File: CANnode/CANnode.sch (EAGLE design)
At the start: 245 parts, among them IC1 ISO1050DUB, IC2 ISO1050DUB, Q1 FDV302P, Q3 FDV302P, U1 LM324PW, U10 FT2232HL, U11 93LC56C-I/SN, U2 TPS70445_PWP_24, U3 LM324PW, U4 LM324PW, U5 LM324PW, U6 LM324PW, U7 RM42L432_PZ_100RM42L432_PZ_100, U8 LM324PW, U9 XC2C32A-6CP56C, X1 AS14-35, Y1 12M

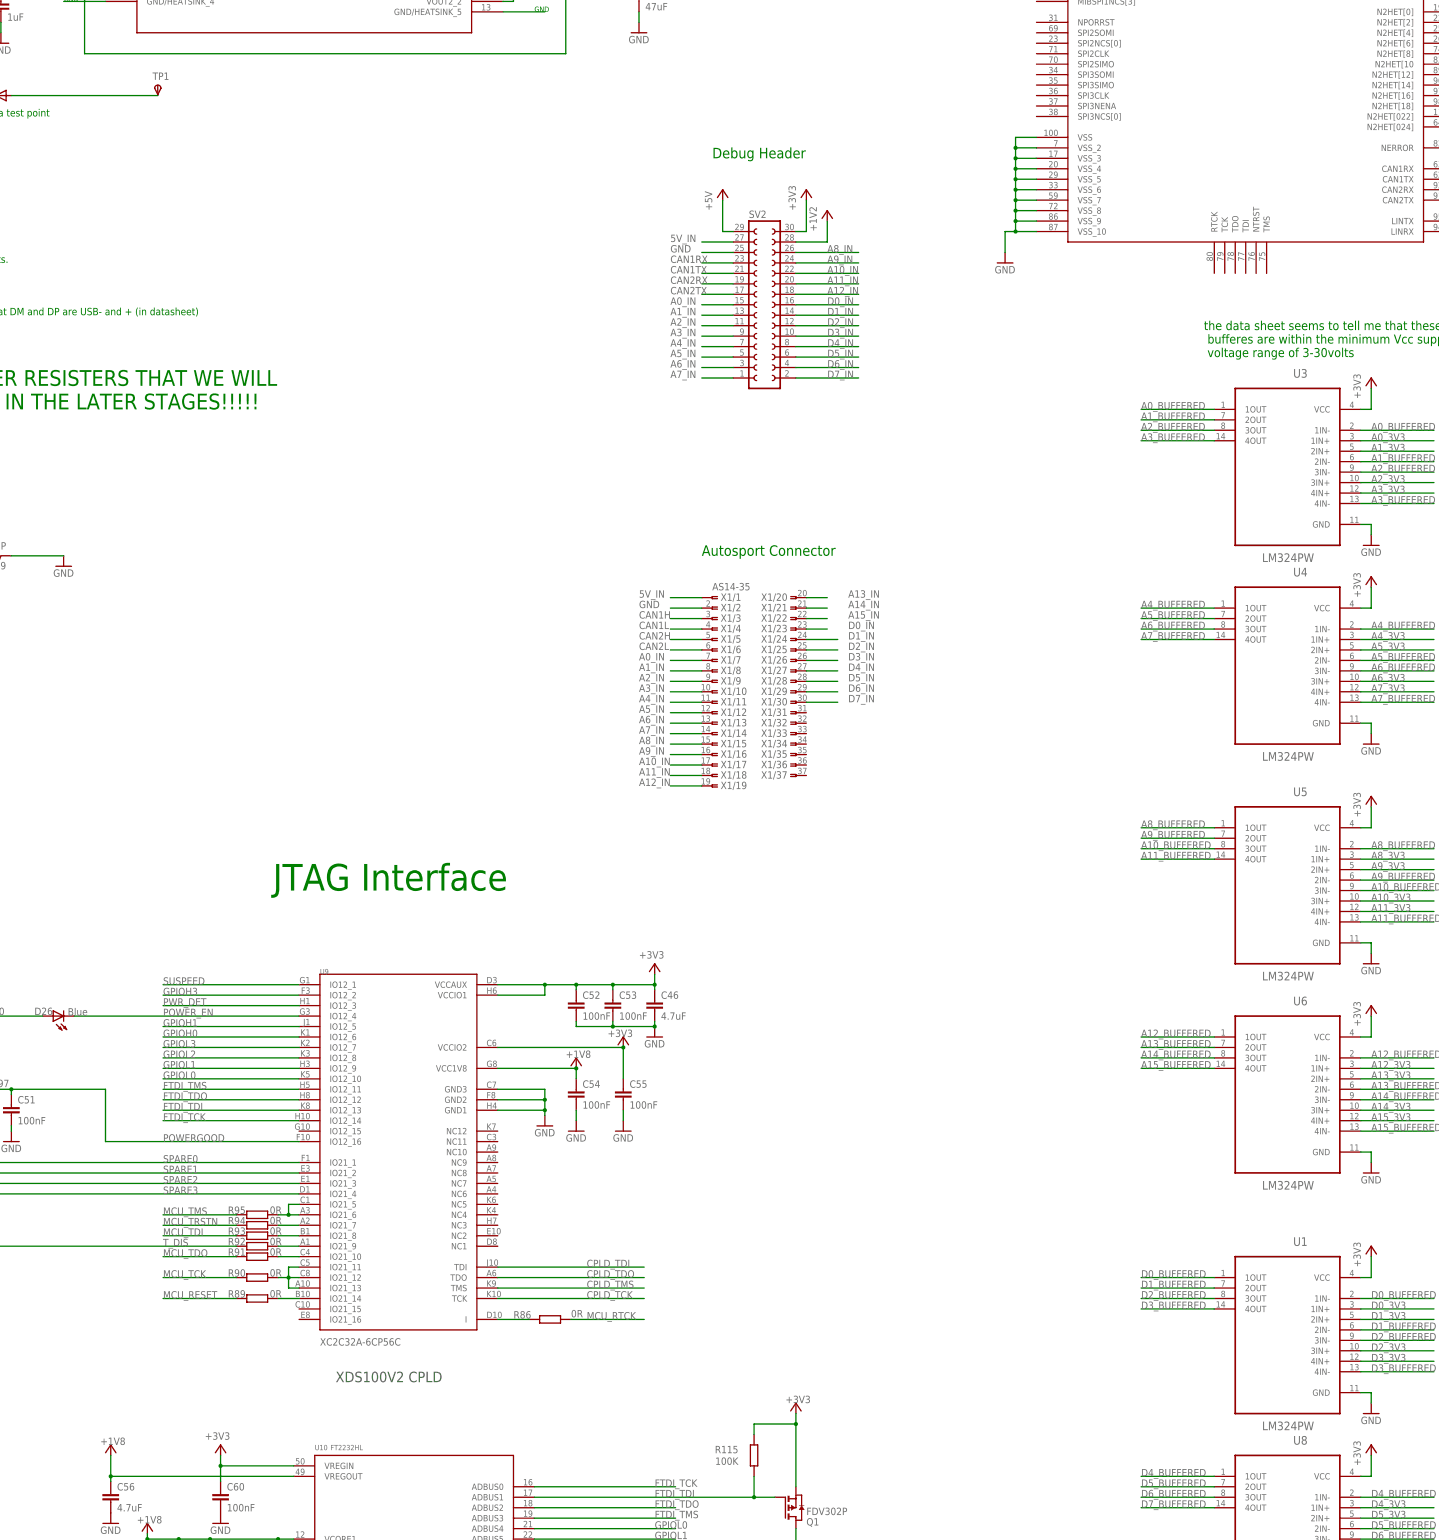
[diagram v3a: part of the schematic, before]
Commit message: played with vias and routing
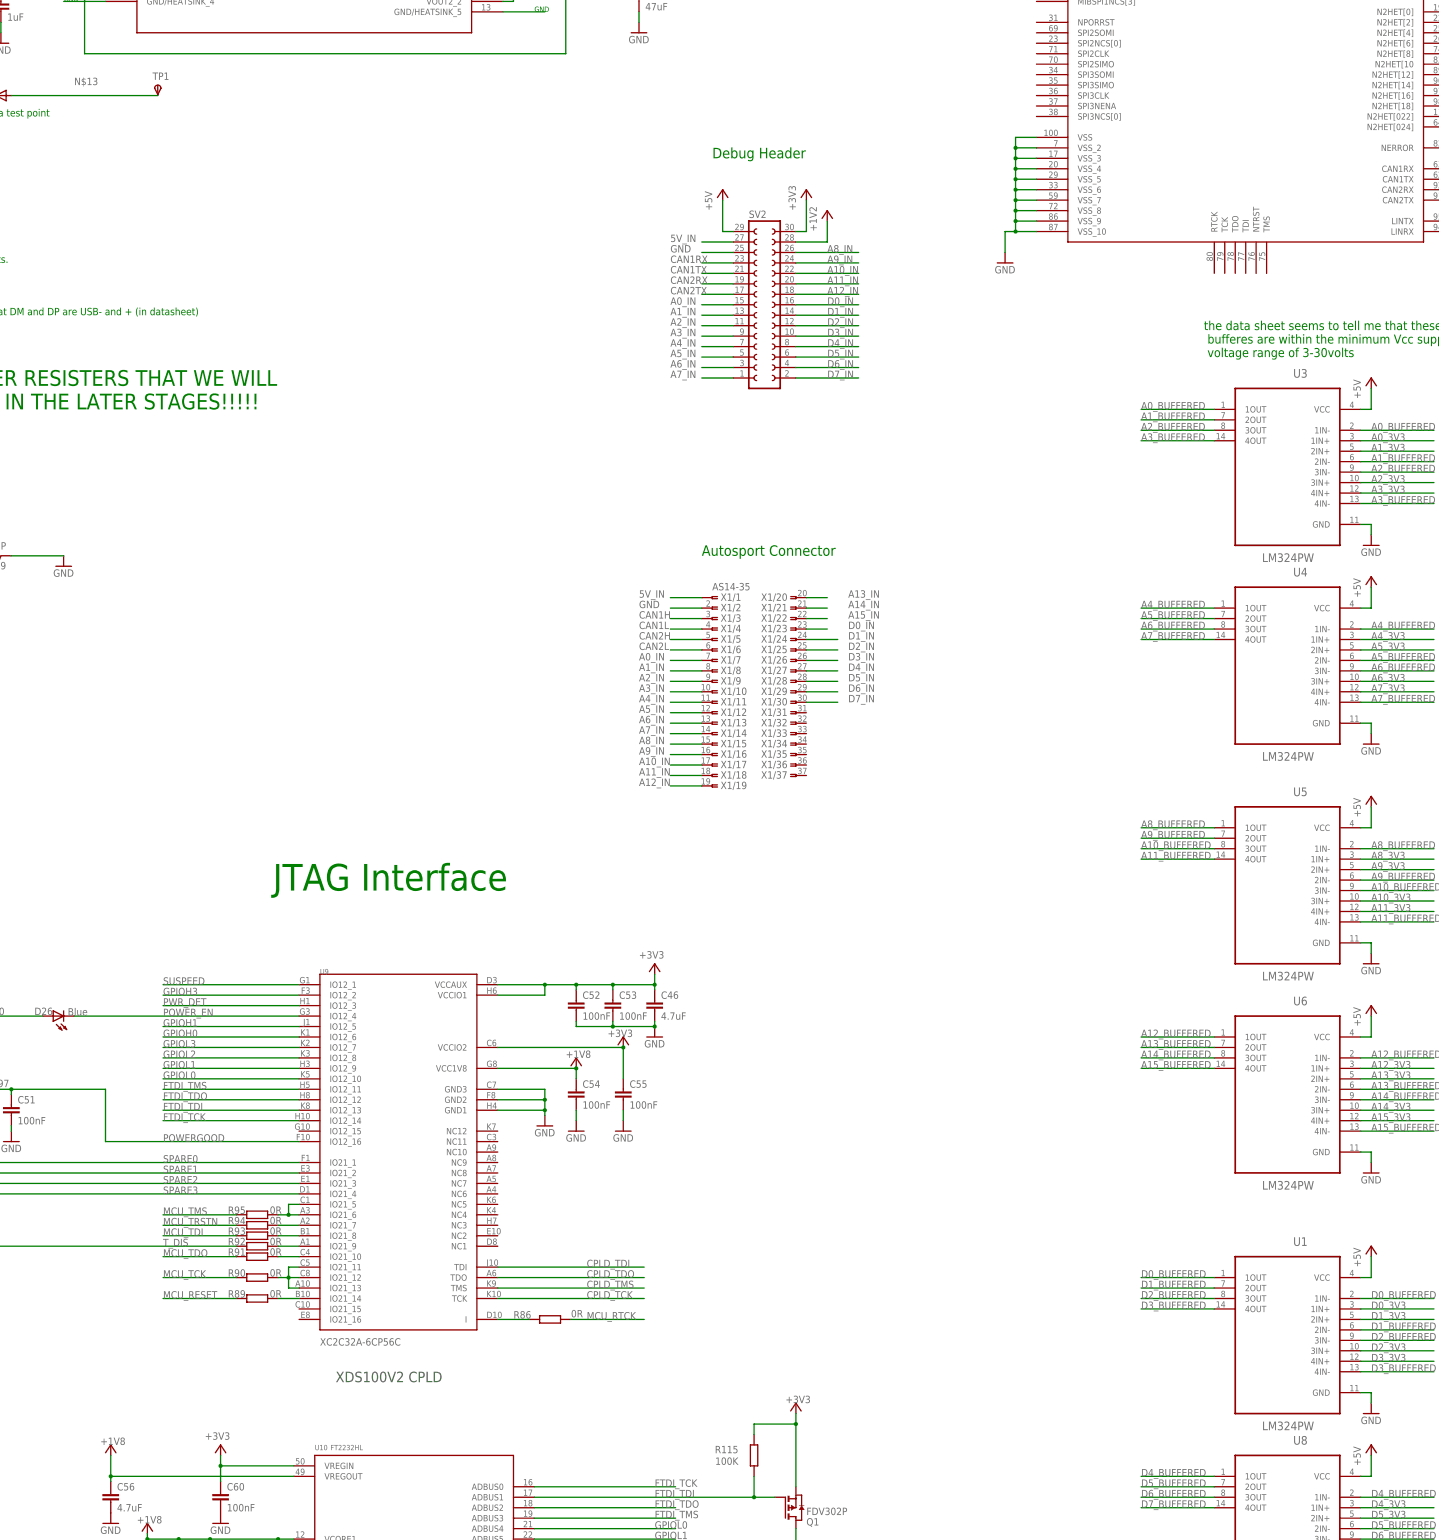
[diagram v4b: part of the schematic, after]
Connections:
- net +3V3: no longer U1.VCC, U3.VCC, U4.VCC, U5.VCC, U6.VCC, U8.VCC
- net +5V: now also U1.VCC, U3.VCC, U4.VCC, U5.VCC, U6.VCC, U8.VCC
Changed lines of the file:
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@@
 <classes>
 <class number="0" name="default" width="0" drill="0">
+<clearance class="0" value="0.205"/>
 </class>
 </classes>
@@
 <part name="GND12" library="supply1" deviceset="GND" device=""/>
 <part name="GND14" library="supply1" deviceset="GND" device=""/>
-<part name="+3V7" library="supply1" deviceset="+3V3" device=""/>
-<part name="+3V8" library="supply1" deviceset="+3V3" device=""/>
-<part name="+3V11" library="supply1" deviceset="+3V3" device=""/>
-<part name="+3V12" library="supply1" deviceset="+3V3" device=""/>
-<part name="+3V13" library="supply1" deviceset="+3V3" device=""/>
-<part name="+3V9" library="supply1" deviceset="+3V3" device=""/>
 <part name="D2" library="eagle-ltspice" deviceset="R" device="R0402" value="TVS DIODE"/>
 <part name="D3" library="eagle-ltspice" deviceset="R" device="R0402" value="TVS DIODE"/>
@@
 <part name="R59" library="resistor" deviceset="R-US_" device="R0402" value="DNP"/>
 <part name="GND120" library="supply1" deviceset="GND" device=""/>
+<part name="P+5" library="supply1" deviceset="+5V" device=""/>
+<part name="P+6" library="supply1" deviceset="+5V" device=""/>
+<part name="P+7" library="supply1" deviceset="+5V" device=""/>
+<part name="P+9" library="supply1" deviceset="+5V" device=""/>
+<part name="P+10" library="supply1" deviceset="+5V" device=""/>
+<part name="P+11" library="supply1" deviceset="+5V" device=""/>
 </parts>
 <sheets>
@@
 <instance part="GND12" gate="1" x="497.84" y="-33.02"/>
 <instance part="GND14" gate="1" x="469.9" y="-50.8"/>
-<instance part="+3V7" gate="G$1" x="411.48" y="-101.6"/>
-<instance part="+3V8" gate="G$1" x="411.48" y="-149.86"/>
-<instance part="+3V11" gate="G$1" x="411.48" y="-254"/>
-<instance part="+3V12" gate="G$1" x="411.48" y="-312.42"/>
-<instance part="+3V13" gate="G$1" x="411.48" y="-360.68"/>
-<instance part="+3V9" gate="G$1" x="411.48" y="-203.2"/>
 <instance part="D2" gate="G$1" x="10.16" y="-96.52" rot="R90"/>
 <instance part="D3" gate="G$1" x="17.78" y="-96.52" rot="R90"/>
@@
 <instance part="R59" gate="G$1" x="76.2" y="-144.78" rot="R180"/>
 <instance part="GND120" gate="1" x="93.98" y="-147.32"/>
+<instance part="P+5" gate="1" x="411.48" y="-101.6"/>
+<instance part="P+6" gate="1" x="411.48" y="-149.86"/>
+<instance part="P+7" gate="1" x="411.48" y="-203.2"/>
+<instance part="P+9" gate="1" x="411.48" y="-254"/>
+<instance part="P+10" gate="1" x="411.48" y="-312.42"/>
+<instance part="P+11" gate="1" x="411.48" y="-360.68"/>
 </instances>
 <busses>
@@
 </segment>
 <segment>
-<pinref part="U3" gate="A" pin="VCC"/>
-<wire x1="408.94" y1="-109.22" x2="411.48" y2="-109.22" width="0.1524" layer="91"/>
-<wire x1="411.48" y1="-109.22" x2="411.48" y2="-104.14" width="0.1524" layer="91"/>
-<pinref part="+3V7" gate="G$1" pin="+3V3"/>
-</segment>
-<segment>
-<pinref part="U4" gate="A" pin="VCC"/>
-<wire x1="408.94" y1="-157.48" x2="411.48" y2="-157.48" width="0.1524" layer="91"/>
-<wire x1="411.48" y1="-157.48" x2="411.48" y2="-152.4" width="0.1524" layer="91"/>
-<pinref part="+3V8" gate="G$1" pin="+3V3"/>
-</segment>
-<segment>
-<pinref part="U6" gate="A" pin="VCC"/>
-<wire x1="408.94" y1="-261.62" x2="411.48" y2="-261.62" width="0.1524" layer="91"/>
-<wire x1="411.48" y1="-261.62" x2="411.48" y2="-256.54" width="0.1524" layer="91"/>
-<pinref part="+3V11" gate="G$1" pin="+3V3"/>
-</segment>
-<segment>
-<pinref part="U1" gate="A" pin="VCC"/>
-<wire x1="408.94" y1="-320.04" x2="411.48" y2="-320.04" width="0.1524" layer="91"/>
-<wire x1="411.48" y1="-320.04" x2="411.48" y2="-314.96" width="0.1524" layer="91"/>
-<pinref part="+3V12" gate="G$1" pin="+3V3"/>
-</segment>
-<segment>
-<pinref part="U8" gate="A" pin="VCC"/>
-<wire x1="408.94" y1="-368.3" x2="411.48" y2="-368.3" width="0.1524" layer="91"/>
-<wire x1="411.48" y1="-368.3" x2="411.48" y2="-363.22" width="0.1524" layer="91"/>
-<pinref part="+3V13" gate="G$1" pin="+3V3"/>
-</segment>
-<segment>
-<pinref part="U5" gate="A" pin="VCC"/>
-<wire x1="408.94" y1="-210.82" x2="411.48" y2="-210.82" width="0.1524" layer="91"/>
-<wire x1="411.48" y1="-210.82" x2="411.48" y2="-205.74" width="0.1524" layer="91"/>
-<pinref part="+3V9" gate="G$1" pin="+3V3"/>
-</segment>
-<segment>
 <pinref part="+3V10" gate="G$1" pin="+3V3"/>
 <wire x1="274.32" y1="-58.42" x2="274.32" y2="-66.04" width="0.1524" layer="91"/>
@@
 <wire x1="81.28" y1="-33.02" x2="116.84" y2="-33.02" width="0.1524" layer="91"/>
 <pinref part="TP1" gate="G$1" pin="PP"/>
+<label x="96.52" y="-30.48" size="1.778" layer="95"/>
 </segment>
 </net>
@@
 <wire x1="254" y1="-66.04" x2="254" y2="-58.42" width="0.1524" layer="91"/>
 </segment>
+<segment>
+<pinref part="U3" gate="A" pin="VCC"/>
+<wire x1="408.94" y1="-109.22" x2="411.48" y2="-109.22" width="0.1524" layer="91"/>
+<wire x1="411.48" y1="-109.22" x2="411.48" y2="-104.14" width="0.1524" layer="91"/>
+<pinref part="P+5" gate="1" pin="+5V"/>
+</segment>
+<segment>
+<pinref part="U4" gate="A" pin="VCC"/>
+<wire x1="408.94" y1="-157.48" x2="411.48" y2="-157.48" width="0.1524" layer="91"/>
+<wire x1="411.48" y1="-157.48" x2="411.48" y2="-152.4" width="0.1524" layer="91"/>
+<pinref part="P+6" gate="1" pin="+5V"/>
+</segment>
+<segment>
+<pinref part="U5" gate="A" pin="VCC"/>
+<wire x1="408.94" y1="-210.82" x2="411.48" y2="-210.82" width="0.1524" layer="91"/>
+<wire x1="411.48" y1="-210.82" x2="411.48" y2="-205.74" width="0.1524" layer="91"/>
+<pinref part="P+7" gate="1" pin="+5V"/>
+</segment>
+<segment>
+<pinref part="U1" gate="A" pin="VCC"/>
+<wire x1="408.94" y1="-320.04" x2="411.48" y2="-320.04" width="0.1524" layer="91"/>
+<wire x1="411.48" y1="-320.04" x2="411.48" y2="-314.96" width="0.1524" layer="91"/>
+<pinref part="P+10" gate="1" pin="+5V"/>
+</segment>
+<segment>
+<pinref part="U8" gate="A" pin="VCC"/>
+<wire x1="408.94" y1="-368.3" x2="411.48" y2="-368.3" width="0.1524" layer="91"/>
+<wire x1="411.48" y1="-368.3" x2="411.48" y2="-363.22" width="0.1524" layer="91"/>
+<pinref part="P+11" gate="1" pin="+5V"/>
+</segment>
+<segment>
+<pinref part="U6" gate="A" pin="VCC"/>
+<wire x1="408.94" y1="-261.62" x2="411.48" y2="-261.62" width="0.1524" layer="91"/>
+<wire x1="411.48" y1="-261.62" x2="411.48" y2="-256.54" width="0.1524" layer="91"/>
+<pinref part="P+9" gate="1" pin="+5V"/>
+</segment>
 </net>

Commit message: Added another layer (Power)
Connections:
- net +5V: now also C1.1, C2.1, C5.+, C6.1, F1.2, R3.2, U2.VIN1, U2.VIN1_2, U2.VIN2, U2.VIN2_2
- net 3.3V: no longer C1.1, C2.1, C5.+, C6.1, F1.2, R3.2, U2.VIN1, U2.VIN1_2, U2.VIN2, U2.VIN2_2
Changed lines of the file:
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@@
 <pinref part="IC1" gate="G$1" pin="VCC2"/>
-</segment>
-<segment>
-<pinref part="U2" gate="A" pin="VIN1"/>
-<wire x1="104.14" y1="12.7" x2="101.6" y2="12.7" width="0.1524" layer="91"/>
-<pinref part="U2" gate="A" pin="VIN1_2"/>
-<wire x1="101.6" y1="12.7" x2="78.74" y2="12.7" width="0.1524" layer="91"/>
-<wire x1="104.14" y1="15.24" x2="101.6" y2="15.24" width="0.1524" layer="91"/>
-<wire x1="101.6" y1="15.24" x2="101.6" y2="12.7" width="0.1524" layer="91"/>
-<junction x="101.6" y="12.7"/>
-<pinref part="C1" gate="G$1" pin="1"/>
-<pinref part="U2" gate="A" pin="VIN2"/>
-<wire x1="104.14" y1="-7.62" x2="101.6" y2="-7.62" width="0.1524" layer="91"/>
-<pinref part="U2" gate="A" pin="VIN2_2"/>
-<wire x1="101.6" y1="-7.62" x2="78.74" y2="-7.62" width="0.1524" layer="91"/>
-<wire x1="104.14" y1="-5.08" x2="101.6" y2="-5.08" width="0.1524" layer="91"/>
-<wire x1="101.6" y1="-5.08" x2="101.6" y2="-7.62" width="0.1524" layer="91"/>
-<junction x="101.6" y="-7.62"/>
-<pinref part="C2" gate="G$1" pin="1"/>
-<wire x1="78.74" y1="-7.62" x2="68.58" y2="-7.62" width="0.1524" layer="91"/>
-<wire x1="68.58" y1="-7.62" x2="68.58" y2="12.7" width="0.1524" layer="91"/>
-<junction x="78.74" y="-7.62"/>
-<wire x1="78.74" y1="12.7" x2="68.58" y2="12.7" width="0.1524" layer="91"/>
-<junction x="78.74" y="12.7"/>
-<junction x="68.58" y="12.7"/>
-<wire x1="68.58" y1="12.7" x2="50.8" y2="12.7" width="0.1524" layer="91"/>
-<pinref part="F1" gate="G$1" pin="2"/>
-<pinref part="R3" gate="G$1" pin="2"/>
-<wire x1="50.8" y1="12.7" x2="40.64" y2="12.7" width="0.1524" layer="91"/>
-<wire x1="40.64" y1="12.7" x2="30.48" y2="12.7" width="0.1524" layer="91"/>
-<wire x1="30.48" y1="12.7" x2="20.32" y2="12.7" width="0.1524" layer="91"/>
-<wire x1="30.48" y1="10.16" x2="30.48" y2="12.7" width="0.1524" layer="91"/>
-<junction x="30.48" y="12.7"/>
-<pinref part="P+3" gate="1" pin="+5V"/>
-<wire x1="30.48" y1="12.7" x2="30.48" y2="20.32" width="0.1524" layer="91"/>
-<pinref part="C5" gate="G$1" pin="+"/>
-<wire x1="40.64" y1="7.62" x2="40.64" y2="12.7" width="0.1524" layer="91"/>
-<junction x="40.64" y="12.7"/>
-<pinref part="C6" gate="G$1" pin="1"/>
-<wire x1="50.8" y1="7.62" x2="50.8" y2="12.7" width="0.1524" layer="91"/>
-<junction x="50.8" y="12.7"/>
 </segment>
 </net>
@@
 <pinref part="P+9" gate="1" pin="+5V"/>
 </segment>
-</net>
+<segment>
+<pinref part="U2" gate="A" pin="VIN1"/>
+<wire x1="104.14" y1="12.7" x2="101.6" y2="12.7" width="0.1524" layer="91"/>
+<pinref part="U2" gate="A" pin="VIN1_2"/>
+<wire x1="101.6" y1="12.7" x2="78.74" y2="12.7" width="0.1524" layer="91"/>
+<wire x1="104.14" y1="15.24" x2="101.6" y2="15.24" width="0.1524" layer="91"/>
+<wire x1="101.6" y1="15.24" x2="101.6" y2="12.7" width="0.1524" layer="91"/>
+<junction x="101.6" y="12.7"/>
+<pinref part="C1" gate="G$1" pin="1"/>
+<pinref part="U2" gate="A" pin="VIN2"/>
+<wire x1="104.14" y1="-7.62" x2="101.6" y2="-7.62" width="0.1524" layer="91"/>
+<pinref part="U2" gate="A" pin="VIN2_2"/>
+<wire x1="101.6" y1="-7.62" x2="78.74" y2="-7.62" width="0.1524" layer="91"/>
+<wire x1="104.14" y1="-5.08" x2="101.6" y2="-5.08" width="0.1524" layer="91"/>
+<wire x1="101.6" y1="-5.08" x2="101.6" y2="-7.62" width="0.1524" layer="91"/>
+<junction x="101.6" y="-7.62"/>
+<pinref part="C2" gate="G$1" pin="1"/>
+<wire x1="78.74" y1="-7.62" x2="68.58" y2="-7.62" width="0.1524" layer="91"/>
+<wire x1="68.58" y1="-7.62" x2="68.58" y2="12.7" width="0.1524" layer="91"/>
+<junction x="78.74" y="-7.62"/>
+<wire x1="78.74" y1="12.7" x2="68.58" y2="12.7" width="0.1524" layer="91"/>
+<junction x="78.74" y="12.7"/>
+<junction x="68.58" y="12.7"/>
+<wire x1="68.58" y1="12.7" x2="50.8" y2="12.7" width="0.1524" layer="91"/>
+<pinref part="F1" gate="G$1" pin="2"/>
+<pinref part="R3" gate="G$1" pin="2"/>
+<wire x1="50.8" y1="12.7" x2="40.64" y2="12.7" width="0.1524" layer="91"/>
+<wire x1="40.64" y1="12.7" x2="30.48" y2="12.7" width="0.1524" layer="91"/>
+<wire x1="30.48" y1="12.7" x2="20.32" y2="12.7" width="0.1524" layer="91"/>
+<wire x1="30.48" y1="10.16" x2="30.48" y2="12.7" width="0.1524" layer="91"/>
+<junction x="30.48" y="12.7"/>
+<pinref part="P+3" gate="1" pin="+5V"/>
+<wire x1="30.48" y1="12.7" x2="30.48" y2="20.32" width="0.1524" layer="91"/>
+<pinref part="C5" gate="G$1" pin="+"/>
+<wire x1="40.64" y1="7.62" x2="40.64" y2="12.7" width="0.1524" layer="91"/>
+<junction x="40.64" y="12.7"/>
+<pinref part="C6" gate="G$1" pin="1"/>
+<wire x1="50.8" y1="7.62" x2="50.8" y2="12.7" width="0.1524" layer="91"/>
+<junction x="50.8" y="12.7"/>
+</segment>
+</net>

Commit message: Connected +5V
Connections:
- removed net 3.3V: C10.1, C9.1, IC1.VCC2, IC2.VCC2
- net +5V: now also C10.1, C9.1, IC1.VCC2, IC2.VCC2
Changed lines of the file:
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@@
-</segment>
-</net>
-<net name="3.3V" class="0">
-<segment>
-<wire x1="505.46" y1="-40.64" x2="505.46" y2="-20.32" width="0.1524" layer="91"/>
-<pinref part="C10" gate="G$1" pin="1"/>
-<wire x1="505.46" y1="-20.32" x2="497.84" y2="-20.32" width="0.1524" layer="91"/>
-<wire x1="497.84" y1="-20.32" x2="497.84" y2="-22.86" width="0.1524" layer="91"/>
-<pinref part="P+2" gate="1" pin="+5V"/>
-<wire x1="497.84" y1="-20.32" x2="497.84" y2="-17.78" width="0.1524" layer="91"/>
-<junction x="497.84" y="-20.32"/>
-<pinref part="IC2" gate="G$1" pin="VCC2"/>
-<wire x1="502.92" y1="-40.64" x2="505.46" y2="-40.64" width="0.1524" layer="91"/>
-</segment>
-<segment>
-<wire x1="505.46" y1="33.02" x2="505.46" y2="50.8" width="0.1524" layer="91"/>
-<pinref part="C9" gate="G$1" pin="1"/>
-<wire x1="505.46" y1="50.8" x2="513.08" y2="50.8" width="0.1524" layer="91"/>
-<wire x1="513.08" y1="50.8" x2="513.08" y2="45.72" width="0.1524" layer="91"/>
-<pinref part="P+1" gate="1" pin="+5V"/>
-<wire x1="513.08" y1="50.8" x2="513.08" y2="53.34" width="0.1524" layer="91"/>
-<junction x="513.08" y="50.8"/>
-<pinref part="IC1" gate="G$1" pin="VCC2"/>
 </segment>
 </net>
@@
 <junction x="50.8" y="12.7"/>
 </segment>
-</net>
+<segment>
+<wire x1="505.46" y1="33.02" x2="505.46" y2="50.8" width="0.1524" layer="91"/>
+<pinref part="C9" gate="G$1" pin="1"/>
+<wire x1="505.46" y1="50.8" x2="513.08" y2="50.8" width="0.1524" layer="91"/>
+<wire x1="513.08" y1="50.8" x2="513.08" y2="45.72" width="0.1524" layer="91"/>
+<pinref part="P+1" gate="1" pin="+5V"/>
+<wire x1="513.08" y1="50.8" x2="513.08" y2="53.34" width="0.1524" layer="91"/>
+<junction x="513.08" y="50.8"/>
+<pinref part="IC1" gate="G$1" pin="VCC2"/>
+</segment>
+<segment>
+<wire x1="505.46" y1="-40.64" x2="505.46" y2="-20.32" width="0.1524" layer="91"/>
+<pinref part="C10" gate="G$1" pin="1"/>
+<wire x1="505.46" y1="-20.32" x2="497.84" y2="-20.32" width="0.1524" layer="91"/>
+<wire x1="497.84" y1="-20.32" x2="497.84" y2="-22.86" width="0.1524" layer="91"/>
+<pinref part="P+2" gate="1" pin="+5V"/>
+<wire x1="497.84" y1="-20.32" x2="497.84" y2="-17.78" width="0.1524" layer="91"/>
+<junction x="497.84" y="-20.32"/>
+<pinref part="IC2" gate="G$1" pin="VCC2"/>
+<wire x1="502.92" y1="-40.64" x2="505.46" y2="-40.64" width="0.1524" layer="91"/>
+</segment>
+</net>
